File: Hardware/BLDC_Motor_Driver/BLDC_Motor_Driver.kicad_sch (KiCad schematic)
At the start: 0 parts

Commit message: add power and MCU sub sheets
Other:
- added sheet MCU (MCU.kicad_sch)
- added sheet Power_Sheet (Power_Sheet.kicad_sch)
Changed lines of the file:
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@@
 	(generator_version "9.0")
 	(paper "A4")
+	(sheet
+		(at 113.03 55.88)
+		(size 31.75 35.56)
+		(exclude_from_sim no)
+		(in_bom yes)
+		(on_board yes)
+		(dnp no)
+		(fields_autoplaced yes)
+		(stroke
+			(width 0.1524)
+			(type solid)
+		)
+		(fill
+			(color 0 0 0 0.0000)
+		)
+		(property "Sheetname" "MCU"
+			(at 113.03 55.1684 0)
+			(effects
+				(font
+					(size 1.27 1.27)
+				)
+				(justify left bottom)
+			)
+		)
+		(property "Sheetfile" "MCU.kicad_sch"
+			(at 113.03 92.0246 0)
+			(effects
+				(font
+					(size 1.27 1.27)
+				)
+				(justify left top)
+			)
+		)
+		(instances
+			(project "BLDC_Motor_Driver"
+				(path "/e34fda66-7244-4ac9-bbf7-3725f03e688f"
+					(page "3")
+				)
+			)
+		)
+	)
+	(sheet
+		(at 58.42 50.8)
+		(size 30.48 36.83)
+		(exclude_from_sim no)
+		(in_bom yes)
+		(on_board yes)
+		(dnp no)
+		(fields_autoplaced yes)
+		(stroke
+			(width 0.1524)
+			(type solid)
+		)
+		(fill
+			(color 0 0 0 0.0000)
+		)
+		(property "Sheetname" "Power_Sheet"
+			(at 58.42 50.0884 0)
+			(effects
+				(font
+					(size 1.27 1.27)
+				)
+				(justify left bottom)
+			)
+		)
+		(property "Sheetfile" "Power_Sheet.kicad_sch"
+			(at 58.42 88.2146 0)
+			(effects
+				(font
+					(size 1.27 1.27)
+				)
+				(justify left top)
+			)
+		)
+		(instances
+			(project "BLDC_Motor_Driver"
+				(path "/e34fda66-7244-4ac9-bbf7-3725f03e688f"
+					(page "2")
+				)
+			)
+		)
+	)
 	(sheet_instances
 		(path "/"

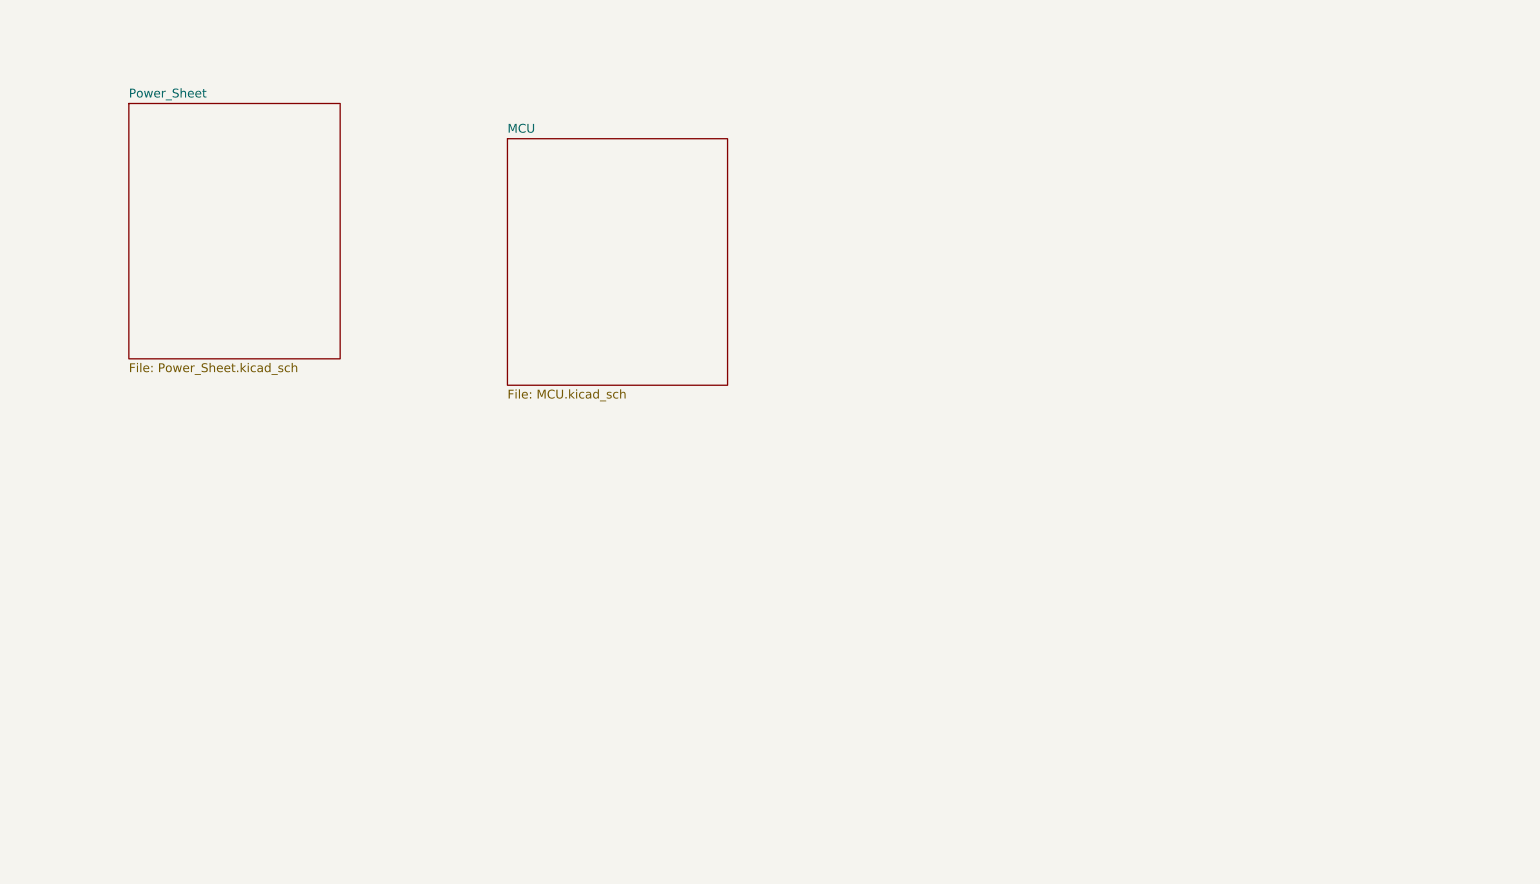
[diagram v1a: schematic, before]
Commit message: Add buck converter IC 36V input to 3.3V
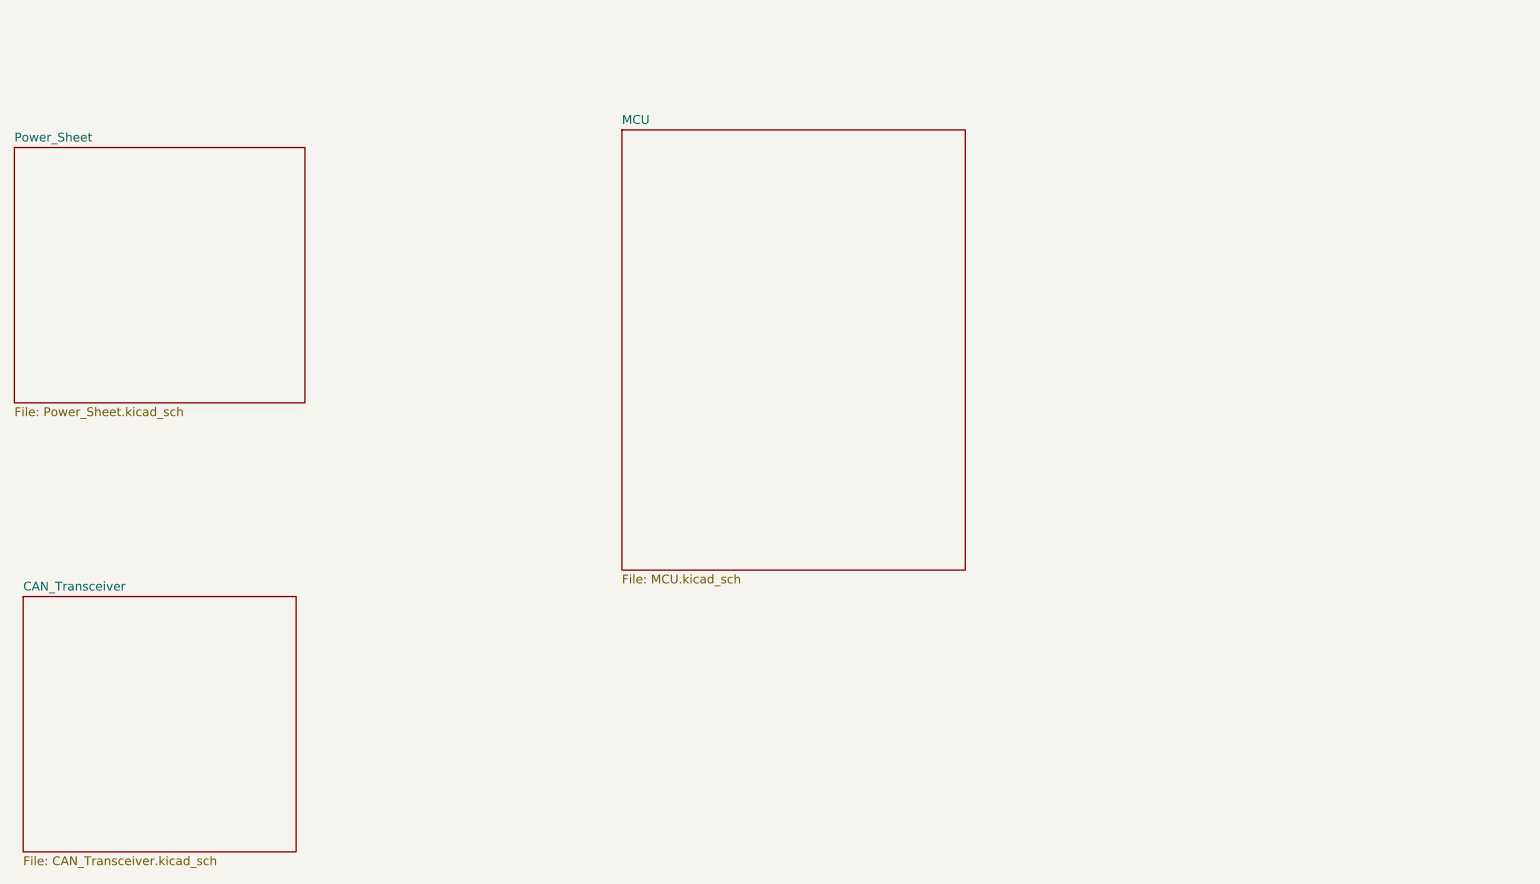
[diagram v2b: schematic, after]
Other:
- added sheet CAN_Transceiver (CAN_Transceiver.kicad_sch)
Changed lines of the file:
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@@
 	(paper "A4")
 	(sheet
-		(at 113.03 55.88)
-		(size 31.75 35.56)
+		(at 43.18 121.92)
+		(size 39.37 36.83)
+		(exclude_from_sim no)
+		(in_bom yes)
+		(on_board yes)
+		(dnp no)
+		(fields_autoplaced yes)
+		(stroke
+			(width 0.1524)
+			(type solid)
+		)
+		(fill
+			(color 0 0 0 0.0000)
+		)
+		(property "Sheetname" "CAN_Transceiver"
+			(at 43.18 121.2084 0)
+			(effects
+				(font
+					(size 1.27 1.27)
+				)
+				(justify left bottom)
+			)
+		)
+		(property "Sheetfile" "CAN_Transceiver.kicad_sch"
+			(at 43.18 159.3346 0)
+			(effects
+				(font
+					(size 1.27 1.27)
+				)
+				(justify left top)
+			)
+		)
+		(instances
+			(project "BLDC_Motor_Driver"
+				(path "/e34fda66-7244-4ac9-bbf7-3725f03e688f"
+					(page "4")
+				)
+			)
+		)
+	)
+	(sheet
+		(at 129.54 54.61)
+		(size 49.53 63.5)
 		(exclude_from_sim no)
 		(in_bom yes)
@@
 		)
 		(property "Sheetname" "MCU"
-			(at 113.03 55.1684 0)
+			(at 129.54 53.8984 0)
 			(effects
 				(font
@@
 		)
 		(property "Sheetfile" "MCU.kicad_sch"
-			(at 113.03 92.0246 0)
+			(at 129.54 118.6946 0)
 			(effects
 				(font
@@
 	)
 	(sheet
-		(at 58.42 50.8)
-		(size 30.48 36.83)
+		(at 41.91 57.15)
+		(size 41.91 36.83)
 		(exclude_from_sim no)
 		(in_bom yes)
@@
 		)
 		(property "Sheetname" "Power_Sheet"
-			(at 58.42 50.0884 0)
+			(at 41.91 56.4384 0)
 			(effects
 				(font
@@
 		)
 		(property "Sheetfile" "Power_Sheet.kicad_sch"
-			(at 58.42 88.2146 0)
+			(at 41.91 94.5646 0)
 			(effects
 				(font

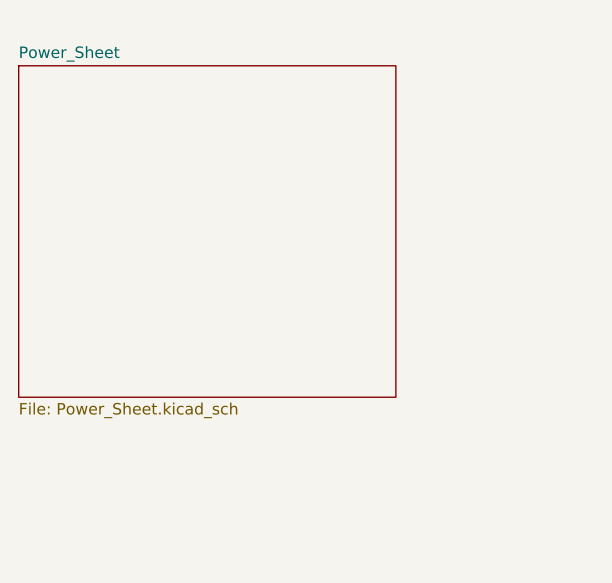
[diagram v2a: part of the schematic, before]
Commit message: Add Selection of CAN IC and arrange the sheet of buck converter
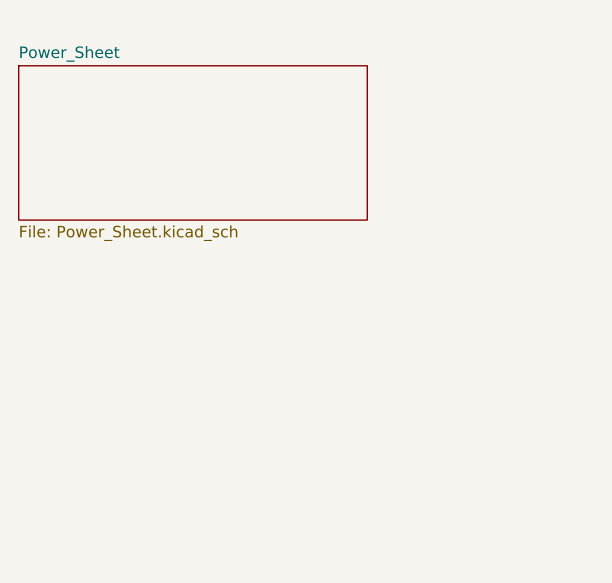
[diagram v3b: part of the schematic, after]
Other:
- title: (none) -> ${Project_Name}
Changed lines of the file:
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@@
 	(generator_version "9.0")
 	(paper "A4")
+	(title_block
+		(title "${Project_Name}")
+		(date "2026-01-05")
+		(rev "V1")
+	)
 	(sheet
 		(at 43.18 121.92)
@@
 	(sheet
 		(at 41.91 57.15)
-		(size 41.91 36.83)
+		(size 38.735 17.145)
 		(exclude_from_sim no)
 		(in_bom yes)
@@
 		)
 		(property "Sheetfile" "Power_Sheet.kicad_sch"
-			(at 41.91 94.5646 0)
+			(at 41.91 74.8796 0)
 			(effects
 				(font

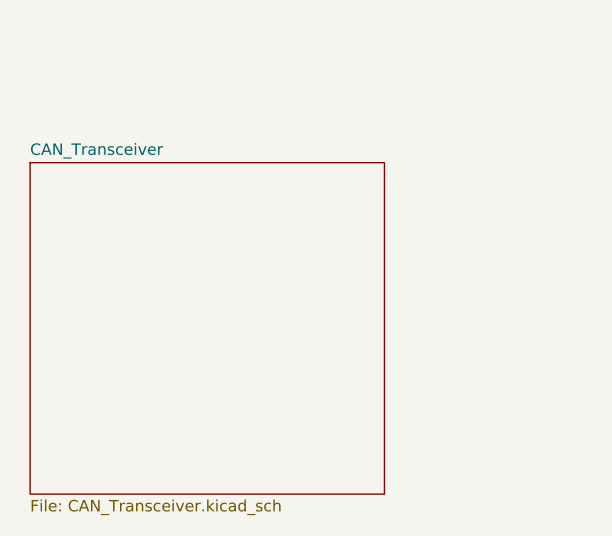
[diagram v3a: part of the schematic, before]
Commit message: Complete CAN IC sheet
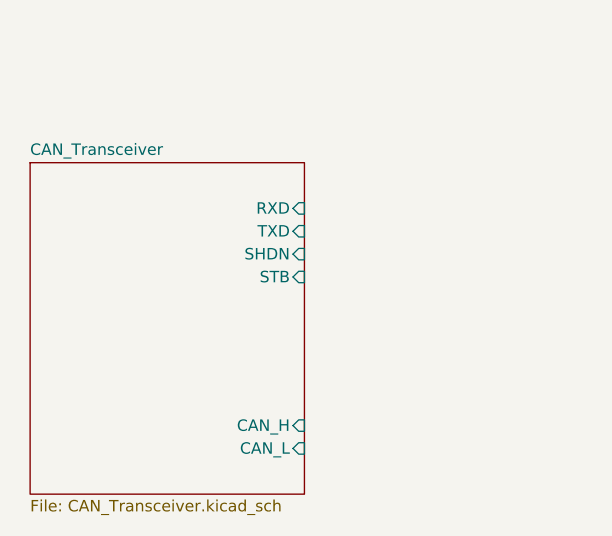
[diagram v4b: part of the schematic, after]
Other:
- sheet CAN_Transceiver ports: added CAN_H, CAN_L, RXD, SHDN, STB, TXD; removed none
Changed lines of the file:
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@@
 	(sheet
 		(at 43.18 121.92)
-		(size 39.37 36.83)
+		(size 30.48 36.83)
 		(exclude_from_sim no)
 		(in_bom yes)
@@
 			)
 		)
+		(pin "CAN_L" input
+			(at 73.66 153.67 0)
+			(effects
+				(font
+					(size 1.27 1.27)
+				)
+				(justify right)
+			)
+		)
+		(pin "CAN_H" input
+			(at 73.66 151.13 0)
+			(effects
+				(font
+					(size 1.27 1.27)
+				)
+				(justify right)
+			)
+		)
+		(pin "RXD" input
+			(at 73.66 127 0)
+			(effects
+				(font
+					(size 1.27 1.27)
+				)
+				(justify right)
+			)
+		)
+		(pin "TXD" input
+			(at 73.66 129.54 0)
+			(effects
+				(font
+					(size 1.27 1.27)
+				)
+				(justify right)
+			)
+		)
+		(pin "SHDN" input
+			(at 73.66 132.08 0)
+			(effects
+				(font
+					(size 1.27 1.27)
+				)
+				(justify right)
+			)
+		)
+		(pin "STB" input
+			(at 73.66 134.62 0)
+			(effects
+				(font
+					(size 1.27 1.27)
+				)
+				(justify right)
+			)
+		)

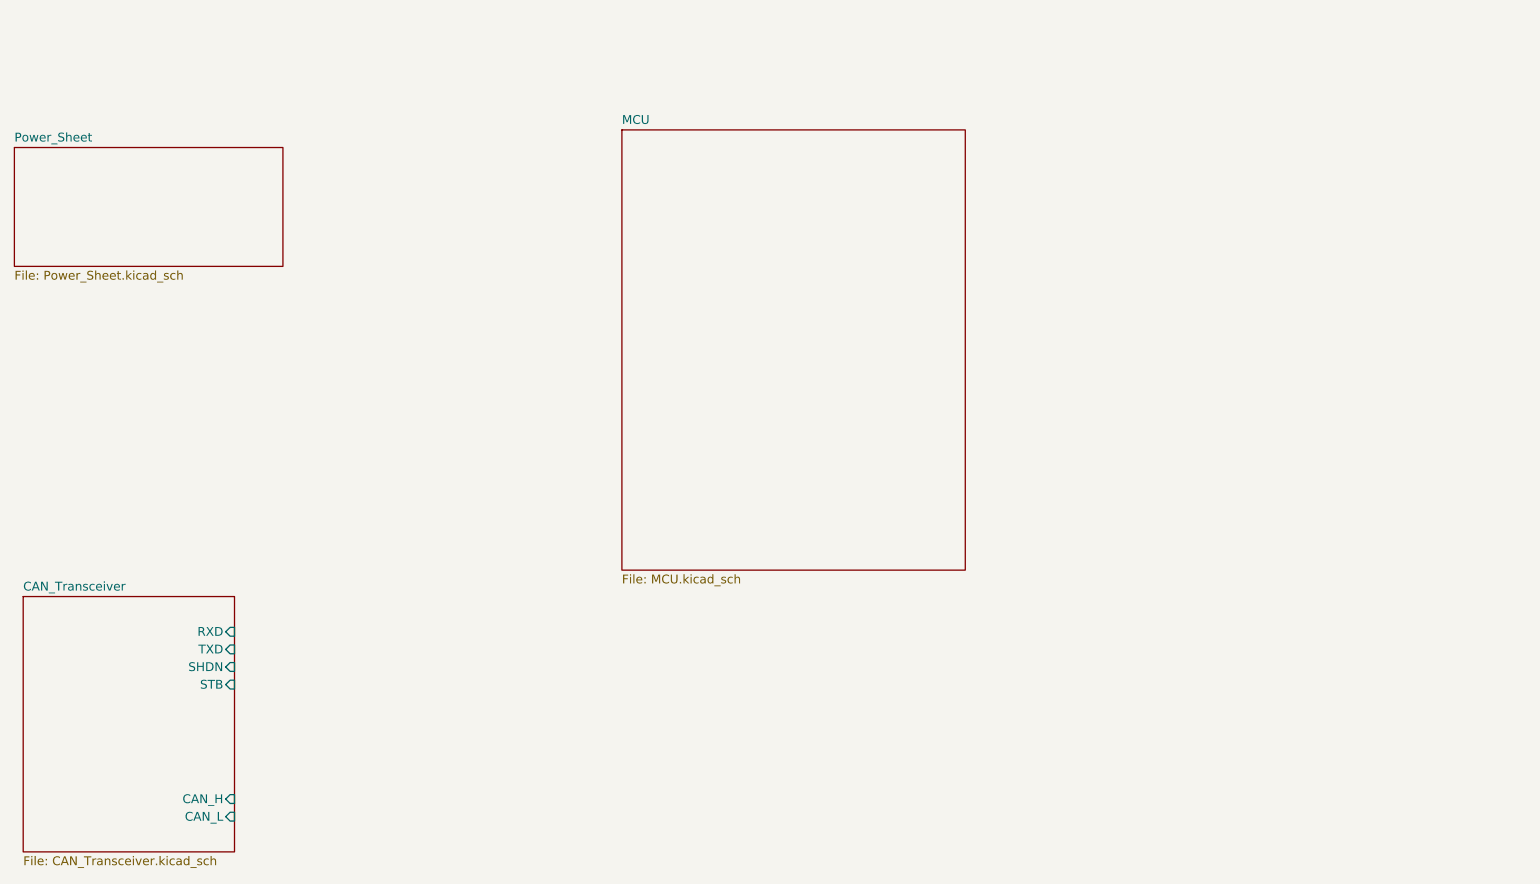
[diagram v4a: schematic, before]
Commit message: Add the EEPROM memory sheet and finish the circuit of it
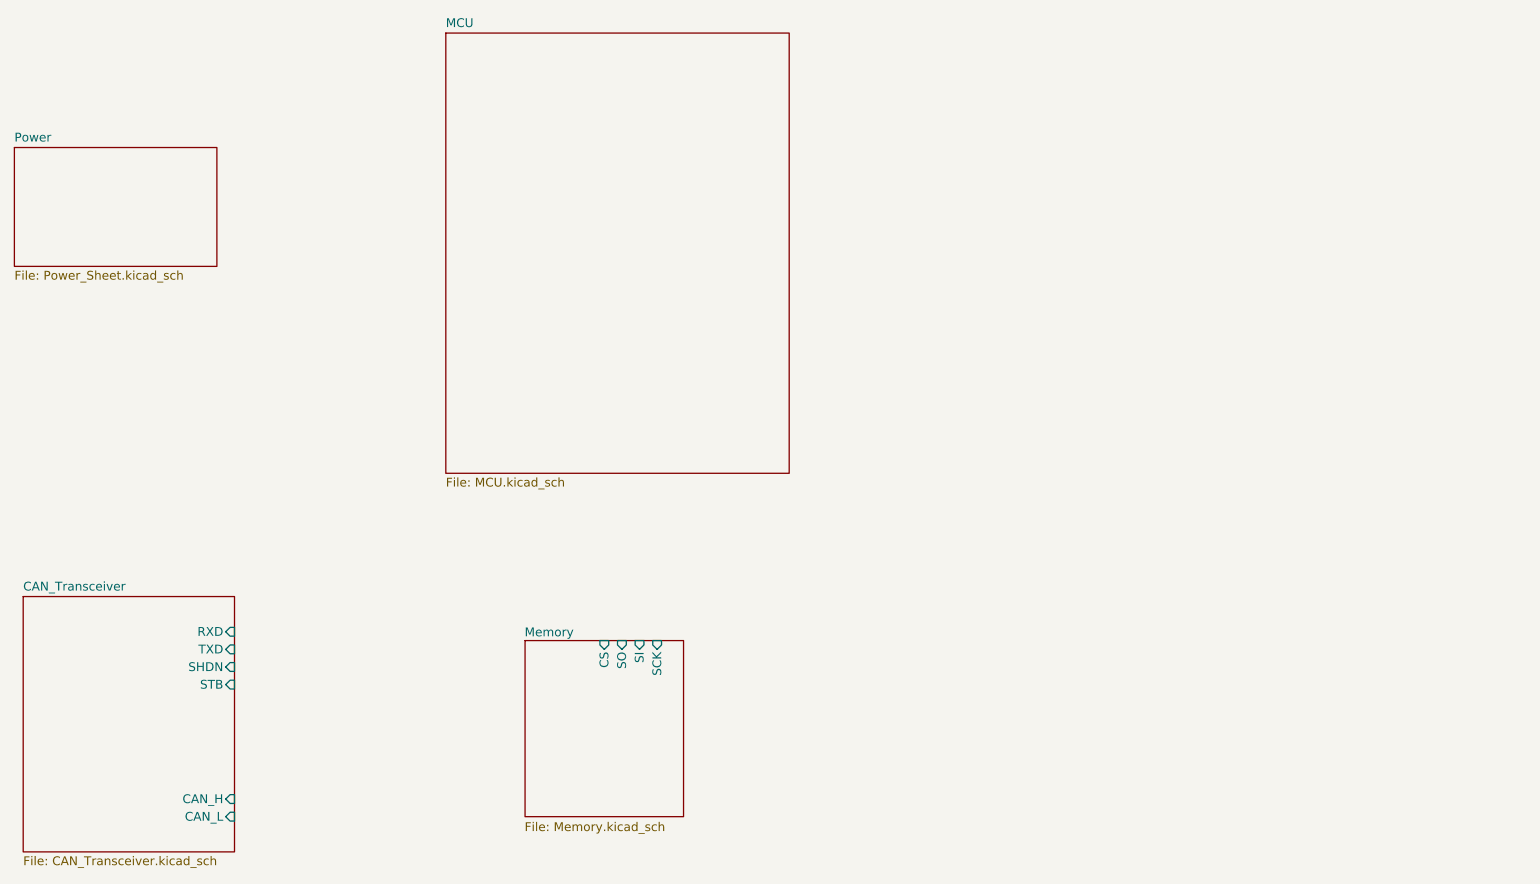
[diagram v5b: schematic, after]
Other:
- sheet Power_Sheet renamed Power
- added sheet Memory (Memory.kicad_sch)
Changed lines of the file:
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@@
 	)
 	(sheet
-		(at 129.54 54.61)
+		(at 104.14 40.64)
 		(size 49.53 63.5)
 		(exclude_from_sim no)
@@
 		)
 		(property "Sheetname" "MCU"
-			(at 129.54 53.8984 0)
+			(at 104.14 39.9284 0)
 			(effects
 				(font
@@
 		)
 		(property "Sheetfile" "MCU.kicad_sch"
-			(at 129.54 118.6946 0)
+			(at 104.14 104.7246 0)
 			(effects
 				(font
@@
 	)
 	(sheet
+		(at 115.57 128.27)
+		(size 22.86 25.4)
+		(exclude_from_sim no)
+		(in_bom yes)
+		(on_board yes)
+		(dnp no)
+		(stroke
+			(width 0.1524)
+			(type solid)
+		)
+		(fill
+			(color 0 0 0 0.0000)
+		)
+		(property "Sheetname" "Memory"
+			(at 115.5043 127.8101 0)
+			(effects
+				(font
+					(size 1.27 1.27)
+				)
+				(justify left bottom)
+			)
+		)
+		(property "Sheetfile" "Memory.kicad_sch"
+			(at 115.5043 154.4144 0)
+			(effects
+				(font
+					(size 1.27 1.27)
+				)
+				(justify left top)
+			)
+		)
+		(pin "SO" input
+			(at 129.54 128.27 90)
+			(effects
+				(font
+					(size 1.27 1.27)
+				)
+				(justify right)
+			)
+		)
+		(pin "CS" input
+			(at 127 128.27 90)
+			(effects
+				(font
+					(size 1.27 1.27)
+				)
+				(justify right)
+			)
+		)
+		(pin "SI" input
+			(at 132.08 128.27 90)
+			(effects
+				(font
+					(size 1.27 1.27)
+				)
+				(justify right)
+			)
+		)
+		(pin "SCK" input
+			(at 134.62 128.27 90)
+			(effects
+				(font
+					(size 1.27 1.27)
+				)
+				(justify right)
+			)
+		)
+		(instances
+			(project "BLDC_Motor_Driver"
+				(path "/e34fda66-7244-4ac9-bbf7-3725f03e688f"
+					(page "5")
+				)
+			)
+		)
+	)
+	(sheet
 		(at 41.91 57.15)
-		(size 38.735 17.145)
+		(size 29.21 17.145)
 		(exclude_from_sim no)
 		(in_bom yes)
@@
 			(color 0 0 0 0.0000)
 		)
-		(property "Sheetname" "Power_Sheet"
+		(property "Sheetname" "Power"
 			(at 41.91 56.4384 0)
 			(effects
